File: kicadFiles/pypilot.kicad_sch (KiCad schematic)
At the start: 51 parts, among them J1 Power +12V, J10 PiZero W, J11 Motor B, J12 GND, J13 GND, J2 Power 0V, J3 2x6, J4 12V, J5 12V, J6 1x4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

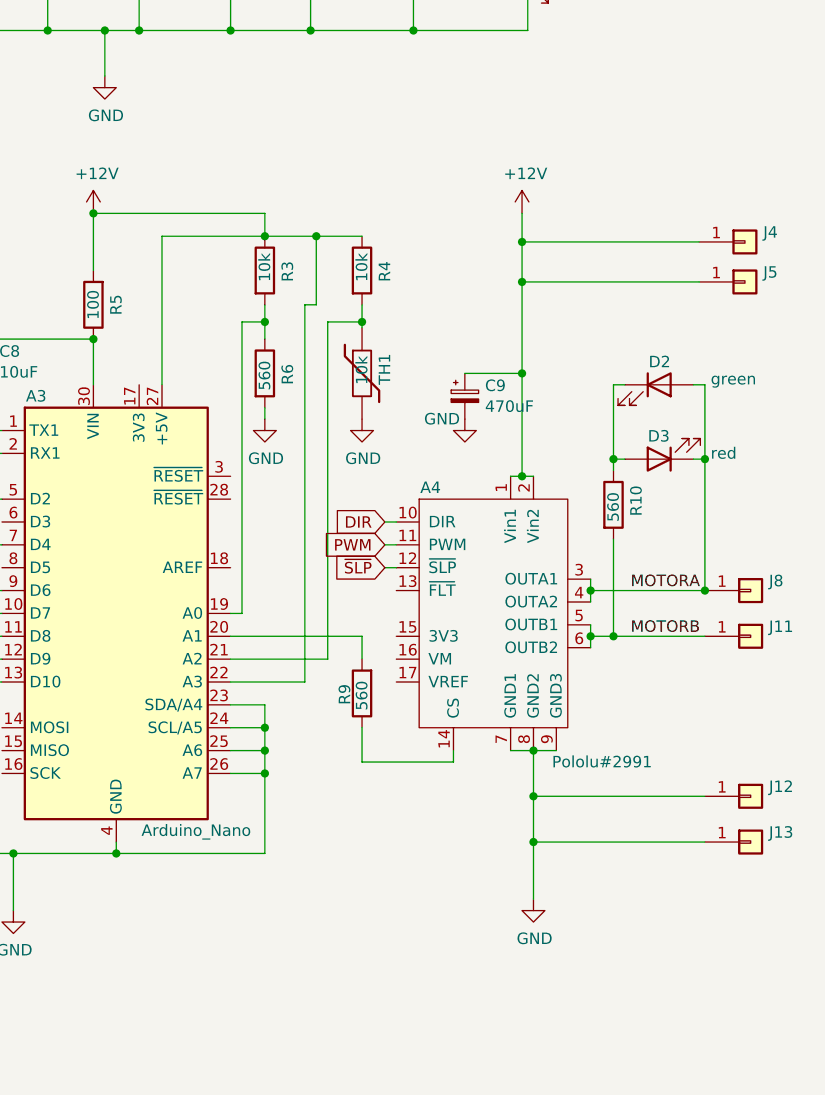
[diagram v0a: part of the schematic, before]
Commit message: 2nd Fix Problem where motor wrongly report 170°C due to error in wiring
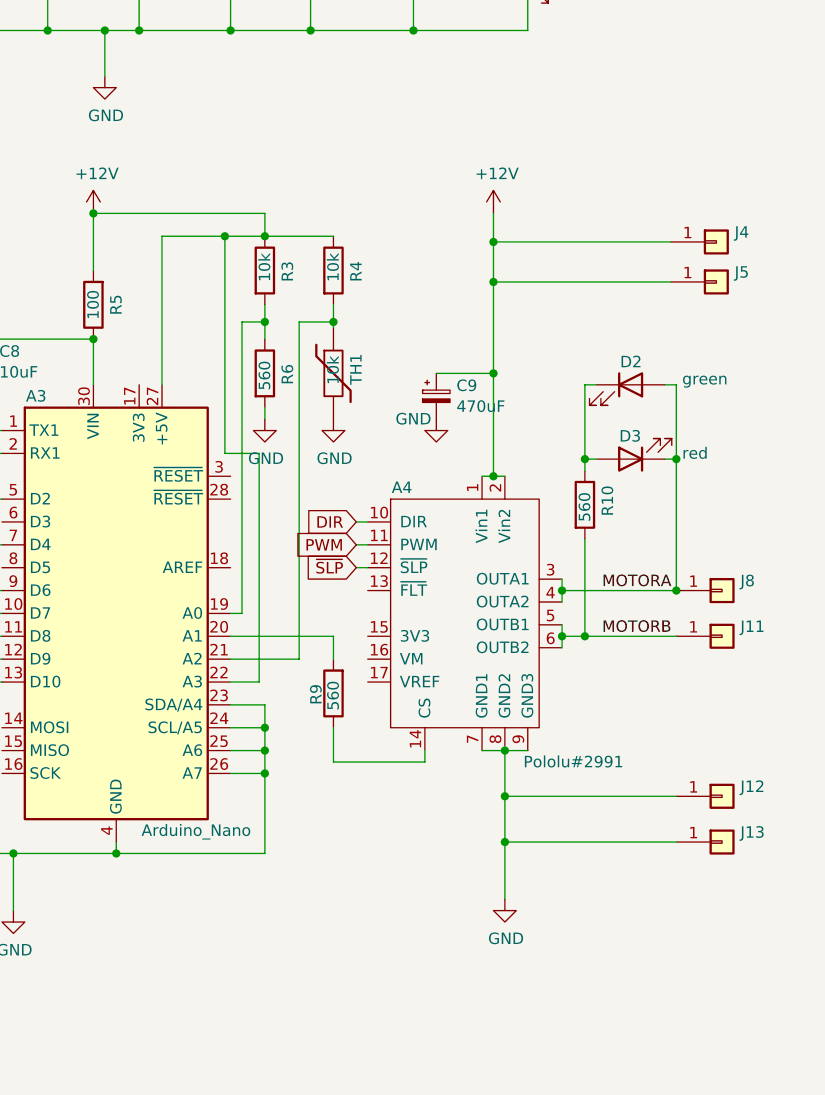
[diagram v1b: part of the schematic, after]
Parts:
- Q1: footprint Package_TO_SOT_THT:TO-92_Inline -> Package_TO_SOT_THT:TO-92
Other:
- company: Marco 'Ironman' Bergman  -> Marco 'Ironman' Bergman & Frederic Guilbault
- moved on the sheet: A4, C9, D2, D3, J11, J12, J13, J4, J5, J8, R10, R4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

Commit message: add details to the BOM
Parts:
- BZ1: footprint Buzzer_Beeper:Buzzer_D14mm_H7mm_P10mm -> Buzzer_Beeper:Buzzer_TDK_PS1240P02BT_D12.2mm_H6.5mm
- R2: value R -> 1k
- R7: value R -> 10k
- R8: value R -> 2k2
- TH1: value 10k -> Handle
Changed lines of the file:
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@@
       (effects (font (size 1.27 1.27)) hide)
     )
-    (property "Datasheet" "" (id 3) (at 57.785 34.925 0)
+    (property "Datasheet" "Mini-360 DC-DC Buck Converter" (id 3) (at 57.785 34.925 0)
       (effects (font (size 1.27 1.27)) hide)
     )
@@
       (effects (font (size 1.27 1.27)) hide)
     )
-    (property "Datasheet" "" (id 3) (at 23.495 114.3 0)
+    (property "Datasheet" "MPU9255 3-axis gyroscope, 3-axis accelerometer, and 3-axis compass/magnetometer" (id 3) (at 23.495 114.3 0)
       (effects (font (size 1.27 1.27)) hide)
     )
@@
       (effects (font (size 1.27 1.27)) hide)
     )
-    (property "Datasheet" "" (id 3) (at 238.125 111.76 0)
+    (property "Datasheet" "Pololu G2 High Power Motor Driver 17A, 6.5V-30V " (id 3) (at 238.125 111.76 0)
       (effects (font (size 1.27 1.27)) hide)
     )
@@
     (in_bom yes) (on_board yes)
     (property "Reference" "R2" (id 0) (at 160.655 48.0822 90))
-    (property "Value" "R" (id 1) (at 160.655 50.3936 90))
+    (property "Value" "1k" (id 1) (at 160.655 50.3936 90))
     (property "Footprint" "Resistor_THT:R_Axial_DIN0309_L9.0mm_D3.2mm_P12.70mm_Horizontal" (id 2) (at 160.655 51.562 90)
       (effects (font (size 1.27 1.27)) hide)
@@
       (effects (font (size 1.27 1.27)) (justify left))
     )
-    (property "Footprint" "Buzzer_Beeper:Buzzer_D14mm_H7mm_P10mm" (id 2) (at 173.99 40.64 90)
-      (effects (font (size 1.27 1.27)) hide)
-    )
-    (property "Datasheet" "~" (id 3) (at 173.99 40.64 90)
+    (property "Footprint" "Buzzer_Beeper:Buzzer_TDK_PS1240P02BT_D12.2mm_H6.5mm" (id 2) (at 173.99 40.64 90)
+      (effects (font (size 1.27 1.27)) hide)
+    )
+    (property "Datasheet" "https://cdn.robotshop.com/media/s/spa/rb-spa-1091/pdf/cem-1203-42-.pdf" (id 3) (at 173.99 40.64 90)
       (effects (font (size 1.27 1.27)) hide)
     )
@@
       (effects (font (size 1.27 1.27)) hide)
     )
-    (property "Datasheet" "~" (id 3) (at 90.805 93.98 0)
+    (property "Datasheet" " 100nf or 0.1uf #104" (id 3) (at 90.805 93.98 0)
       (effects (font (size 1.27 1.27)) hide)
     )
@@
       (effects (font (size 1.27 1.27)) hide)
     )
-    (property "Datasheet" "~" (id 3) (at 185.42 97.79 0)
+    (property "Datasheet" " 100nf or 0.1uf #104" (id 3) (at 185.42 97.79 0)
       (effects (font (size 1.27 1.27)) hide)
     )
@@
       (effects (font (size 1.27 1.27)) hide)
     )
-    (property "Datasheet" "~" (id 3) (at 79.375 46.355 0)
+    (property "Datasheet" " 100nf or 0.1uf #104" (id 3) (at 79.375 46.355 0)
       (effects (font (size 1.27 1.27)) hide)
     )
@@
       (effects (font (size 1.27 1.27)) hide)
     )
-    (property "Datasheet" "~" (id 3) (at 34.925 46.355 0)
+    (property "Datasheet" " 100nf or 0.1uf #104" (id 3) (at 34.925 46.355 0)
       (effects (font (size 1.27 1.27)) hide)
     )
@@
       (effects (font (size 1.27 1.27)) (justify left))
     )
-    (property "Value" "R" (id 1) (at 130.683 111.633 0)
+    (property "Value" "10k" (id 1) (at 130.683 111.633 0)
       (effects (font (size 1.27 1.27)) (justify left))
     )
@@
       (effects (font (size 1.27 1.27)) (justify left))
     )
-    (property "Value" "R" (id 1) (at 130.683 119.253 0)
+    (property "Value" "2k2" (id 1) (at 130.683 119.253 0)
       (effects (font (size 1.27 1.27)) (justify left))
     )
@@
       (effects (font (size 1.27 1.27)) hide)
     )
-    (property "Datasheet" "~" (id 3) (at 192.405 97.79 0)
+    (property "Datasheet" "" (id 3) (at 192.405 97.79 0)
       (effects (font (size 1.27 1.27)) hide)
     )
@@
       (effects (font (size 1.27 1.27)) hide)
     )
-    (property "Datasheet" "~" (id 3) (at 97.79 93.98 0)
+    (property "Datasheet" "" (id 3) (at 97.79 93.98 0)
       (effects (font (size 1.27 1.27)) hide)
     )
@@
       (effects (font (size 1.27 1.27)) hide)
     )
-    (property "Datasheet" "~" (id 3) (at 71.755 46.355 0)
+    (property "Datasheet" "" (id 3) (at 71.755 46.355 0)
       (effects (font (size 1.27 1.27)) hide)
     )
@@
       (effects (font (size 1.27 1.27)) hide)
     )
-    (property "Datasheet" "~" (id 3) (at 38.735 46.355 0)
+    (property "Datasheet" "" (id 3) (at 38.735 46.355 0)
       (effects (font (size 1.27 1.27)) hide)
     )
@@
       (effects (font (size 1.27 1.27)) (justify left))
     )
-    (property "Value" "10k" (id 1) (at 231.775 100.33 90)
+    (property "Value" "Handle" (id 1) (at 231.775 100.33 90)
       (effects (font (size 1.27 1.27)) (justify left))
     )
@@
       (effects (font (size 1.27 1.27)) hide)
     )
-    (property "Datasheet" "~" (id 3) (at 231.775 99.06 0)
+    (property "Datasheet" "This is just an handle to fix the cover on." (id 3) (at 231.775 99.06 0)
       (effects (font (size 1.27 1.27)) hide)
     )
@@
     )
     (path "/00000000-0000-0000-0000-00006295ac9f"
-      (reference "BZ1") (unit 1) (value "Buzzer") (footprint "Buzzer_Beeper:Buzzer_D14mm_H7mm_P10mm")
+      (reference "BZ1") (unit 1) (value "Buzzer") (footprint "Buzzer_Beeper:Buzzer_TDK_PS1240P02BT_D12.2mm_H6.5mm")
     )
     (path "/00000000-0000-0000-0000-00006296a091"
@@
     )
     (path "/00000000-0000-0000-0000-00006295a0d0"
-      (reference "R2") (unit 1) (value "R") (footprint "Resistor_THT:R_Axial_DIN0309_L9.0mm_D3.2mm_P12.70mm_Horizontal")
+      (reference "R2") (unit 1) (value "1k") (footprint "Resistor_THT:R_Axial_DIN0309_L9.0mm_D3.2mm_P12.70mm_Horizontal")
     )
     (path "/00000000-0000-0000-0000-000062bc1c29"
@@
     )
     (path "/00000000-0000-0000-0000-0000629842bd"
-      (reference "R7") (unit 1) (value "R") (footprint "Resistor_THT:R_Axial_DIN0309_L9.0mm_D3.2mm_P12.70mm_Horizontal")
+      (reference "R7") (unit 1) (value "10k") (footprint "Resistor_THT:R_Axial_DIN0309_L9.0mm_D3.2mm_P12.70mm_Horizontal")
     )
     (path "/00000000-0000-0000-0000-000062984756"
-      (reference "R8") (unit 1) (value "R") (footprint "Resistor_THT:R_Axial_DIN0309_L9.0mm_D3.2mm_P12.70mm_Horizontal")
+      (reference "R8") (unit 1) (value "2k2") (footprint "Resistor_THT:R_Axial_DIN0309_L9.0mm_D3.2mm_P12.70mm_Horizontal")
     )
     (path "/00000000-0000-0000-0000-000062ba0a8a"
@@
     )
     (path "/00000000-0000-0000-0000-000062bdd879"
-      (reference "TH1") (unit 1) (value "10k") (footprint "Resistor_THT:R_Axial_DIN0309_L9.0mm_D3.2mm_P5.08mm_Vertical")
-    )
-  )
+      (reference "TH1") (unit 1) (value "Handle") (footprint "Resistor_THT:R_Axial_DIN0309_L9.0mm_D3.2mm_P5.08mm_Vertical")
+    )
+  )
